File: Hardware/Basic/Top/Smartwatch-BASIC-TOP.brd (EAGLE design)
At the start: 38 x 38 mm, 59 parts, among them SW6 SWITCH.MOM, SW7 SWITCH.MOM, U2 NRF52832_MODULE_MDBT42, U4 FT231XS

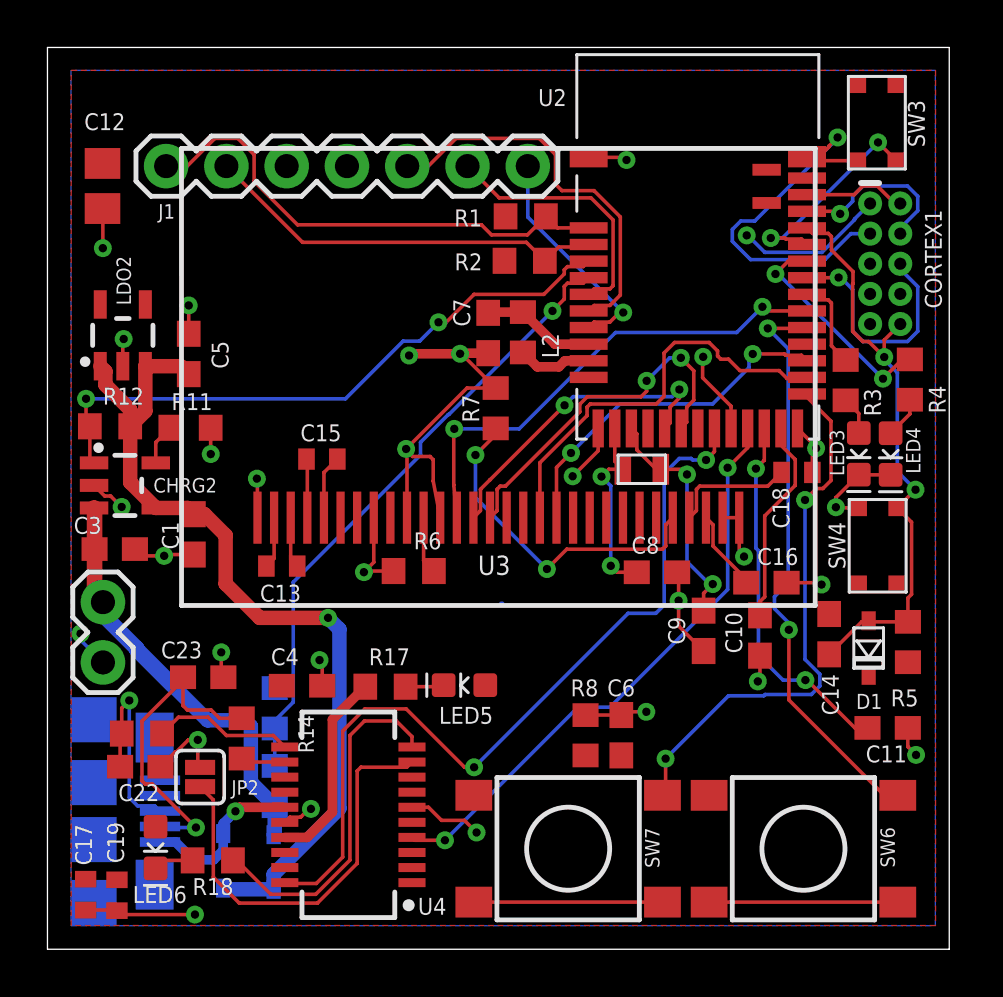
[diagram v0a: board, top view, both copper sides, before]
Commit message: Fixed Top Board Polygon
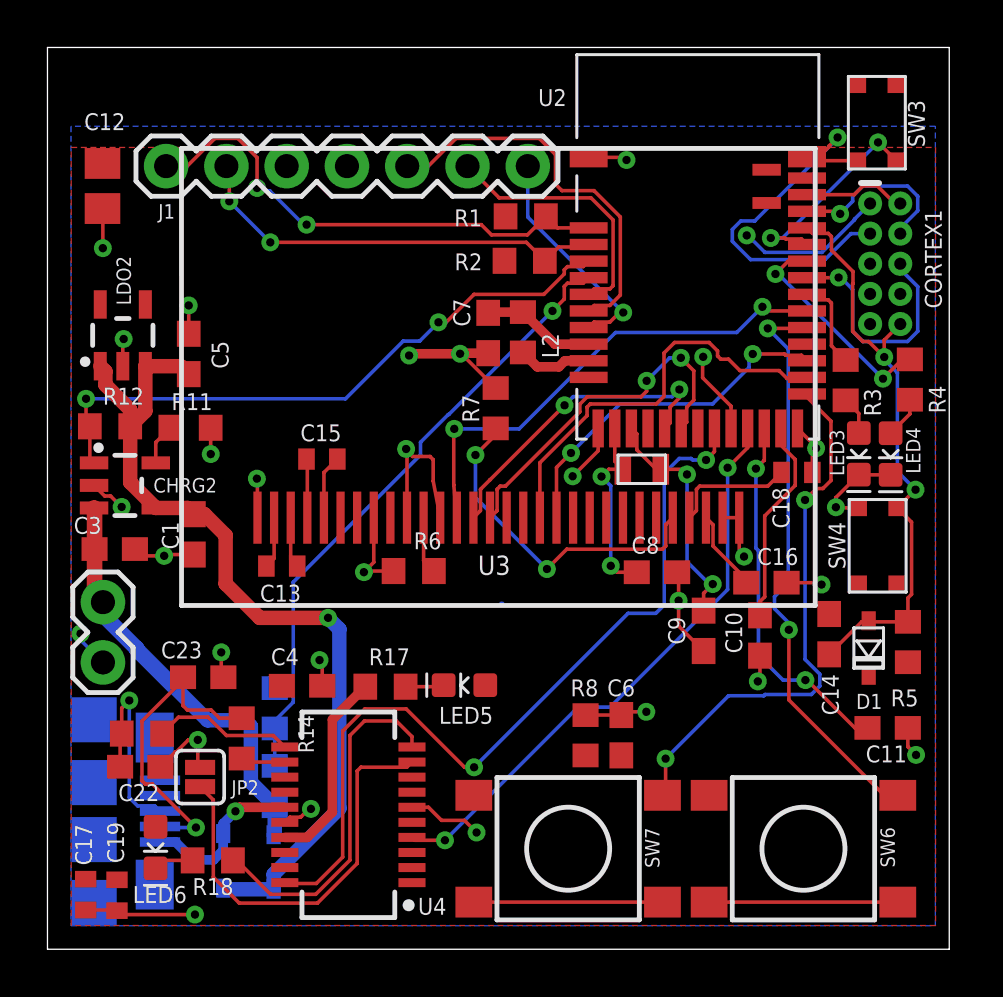
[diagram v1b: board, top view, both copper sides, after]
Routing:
- net GND: track 88.2 -> 83.3 mm
- net SCL: track 17.2 -> 18.0 mm, vias 0 -> 2
- net SDA: vias 0 -> 2
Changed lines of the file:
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@@
 <drawing>
 <settings>
-<setting alwaysvectorfont="yes"/>
+<setting alwaysvectorfont="no"/>
 <setting verticaltext="up"/>
 </settings>
@@
 <wire x1="33.29431875" y1="34.17755625" x2="29.80478125" y2="30.68801875" width="0.1524" layer="16"/>
 <wire x1="29.80478125" y1="30.68801875" x2="29.21519375" y2="30.68801875" width="0.1524" layer="16"/>
-<wire x1="15.113" y1="21.082" x2="17.68004375" y2="23.64904375" width="0.1524" layer="1"/>
-<wire x1="17.68004375" y1="23.64904375" x2="18.887659375" y2="23.64904375" width="0.1524" layer="1"/>
 <wire x1="17.387059375" y1="25.092659375" x2="15.313659375" y2="25.092659375" width="0.4064" layer="1"/>
 <wire x1="15.313659375" y1="25.092659375" x2="15.24" y2="25.019" width="0.4064" layer="1"/>
@@
 <via x="36.601403125" y="8.188959375" extent="1-16" drill="0.35"/>
 <polygon width="0.1524" layer="16" isolate="0.1778">
-<vertex x="0.9906" y="37.0332"/>
+<vertex x="0.9906" y="34.67861875"/>
 <vertex x="0.9906" y="0.9906"/>
 <vertex x="37.4142" y="0.9906"/>
-<vertex x="37.4142" y="37.0332"/>
+<vertex x="37.4142" y="34.67861875"/>
 </polygon>
 <wire x1="31.145615625" y1="15.44699375" x2="32.5386875" y2="15.44699375" width="0.1524" layer="1"/>
@@
 <contactref element="R2" pad="2"/>
 <polygon width="0.1524" layer="1">
-<vertex x="1" y="37.035559375"/>
-<vertex x="37.421640625" y="37.035559375"/>
+<vertex x="1" y="33.786896875"/>
+<vertex x="37.421640625" y="33.786896875"/>
 <vertex x="37.421640625" y="1"/>
 <vertex x="1" y="1"/>
@@
 <contactref element="J1" pad="1"/>
 <wire x1="7.05603125" y1="34.1684" x2="8.02396875" y2="34.1684" width="0.1524" layer="1"/>
-<wire x1="8.02396875" y1="34.1684" x2="8.7084" y2="33.48396875" width="0.1524" layer="1"/>
+<wire x1="8.02396875" y1="34.1684" x2="8.832859375" y2="33.359509375" width="0.1524" layer="1"/>
 <wire x1="5" y1="33" x2="5.88763125" y2="33" width="0.1524" layer="1"/>
 <wire x1="5.88763125" y1="33" x2="7.05603125" y2="34.1684" width="0.1524" layer="1"/>
-<wire x1="8.7084" y1="33.48396875" x2="8.7084" y2="32.35831875" width="0.1524" layer="1"/>
-<wire x1="8.7084" y1="32.35831875" x2="10.53871875" y2="30.528" width="0.1524" layer="1"/>
-<wire x1="18.28631875" y1="30.528" x2="18.70975625" y2="30.1045625" width="0.1524" layer="1"/>
+<wire x1="8.832859375" y1="33.359509375" x2="8.832859375" y2="32.07891875" width="0.1524" layer="1"/>
+<wire x1="10.91971875" y1="30.533078125" x2="10.79525625" y2="30.533078125" width="0.1524" layer="16"/>
+<wire x1="10.79525625" y1="30.533078125" x2="9.373878125" y2="31.95445625" width="0.1524" layer="16"/>
+<wire x1="9.373878125" y1="31.95445625" x2="8.957321875" y2="31.95445625" width="0.1524" layer="16"/>
+<wire x1="8.832859375" y1="32.07891875" x2="8.957321875" y2="31.95445625" width="0.1524" layer="16"/>
+<wire x1="18.281240625" y1="30.533078125" x2="18.70975625" y2="30.1045625" width="0.1524" layer="1"/>
 <wire x1="18.70975625" y1="30.1045625" x2="20.22584375" y2="30.1045625" width="0.1524" layer="1"/>
 <wire x1="20.22584375" y1="30.1045625" x2="21.004440625" y2="30.883159375" width="0.1524" layer="1"/>
-<wire x1="10.53871875" y1="30.528" x2="18.28631875" y2="30.528" width="0.1524" layer="1"/>
+<wire x1="10.91971875" y1="30.533078125" x2="18.281240625" y2="30.533078125" width="0.1524" layer="1"/>
 <wire x1="21.004440625" y1="30.883159375" x2="21.4906" y2="30.397" width="0.1524" layer="1"/>
 <wire x1="21.4906" y1="30.397" x2="22.806" y2="30.397" width="0.1524" layer="1"/>
+<via x="8.832859375" y="32.07891875" extent="1-16" drill="0.35"/>
+<via x="10.91971875" y="30.533078125" extent="1-16" drill="0.35"/>
 </signal>
 <signal name="SCL">
@@
 <contactref element="J1" pad="2"/>
 <wire x1="22.806" y1="29.697" x2="22.7016" y2="29.5926" width="0.1524" layer="1"/>
-<wire x1="7.54" y1="33" x2="10.7512375" y2="29.7887625" width="0.1524" layer="1"/>
+<wire x1="9.389796875" y1="29.7887625" x2="7.66191875" y2="31.516640625" width="0.1524" layer="16"/>
+<wire x1="7.54" y1="33" x2="7.66191875" y2="32.87808125" width="0.1524" layer="1"/>
+<wire x1="7.66191875" y1="32.87808125" x2="7.66191875" y2="31.516640625" width="0.1524" layer="1"/>
 <wire x1="20.180121875" y1="29.7887625" x2="20.958721875" y2="29.0101625" width="0.1524" layer="1"/>
-<wire x1="10.7512375" y1="29.7887625" x2="20.180121875" y2="29.7887625" width="0.1524" layer="1"/>
+<wire x1="9.389796875" y1="29.7887625" x2="20.180121875" y2="29.7887625" width="0.1524" layer="1"/>
 <wire x1="21.541159375" y1="29.5926" x2="20.958721875" y2="29.0101625" width="0.1524" layer="1"/>
 <wire x1="22.7016" y1="29.5926" x2="21.541159375" y2="29.5926" width="0.1524" layer="1"/>
+<via x="9.389796875" y="29.7887625" extent="1-16" drill="0.35"/>
+<via x="7.66191875" y="31.516640625" extent="1-16" drill="0.35"/>
 </signal>
 <signal name="SCK">

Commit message: Top board fixed some traces
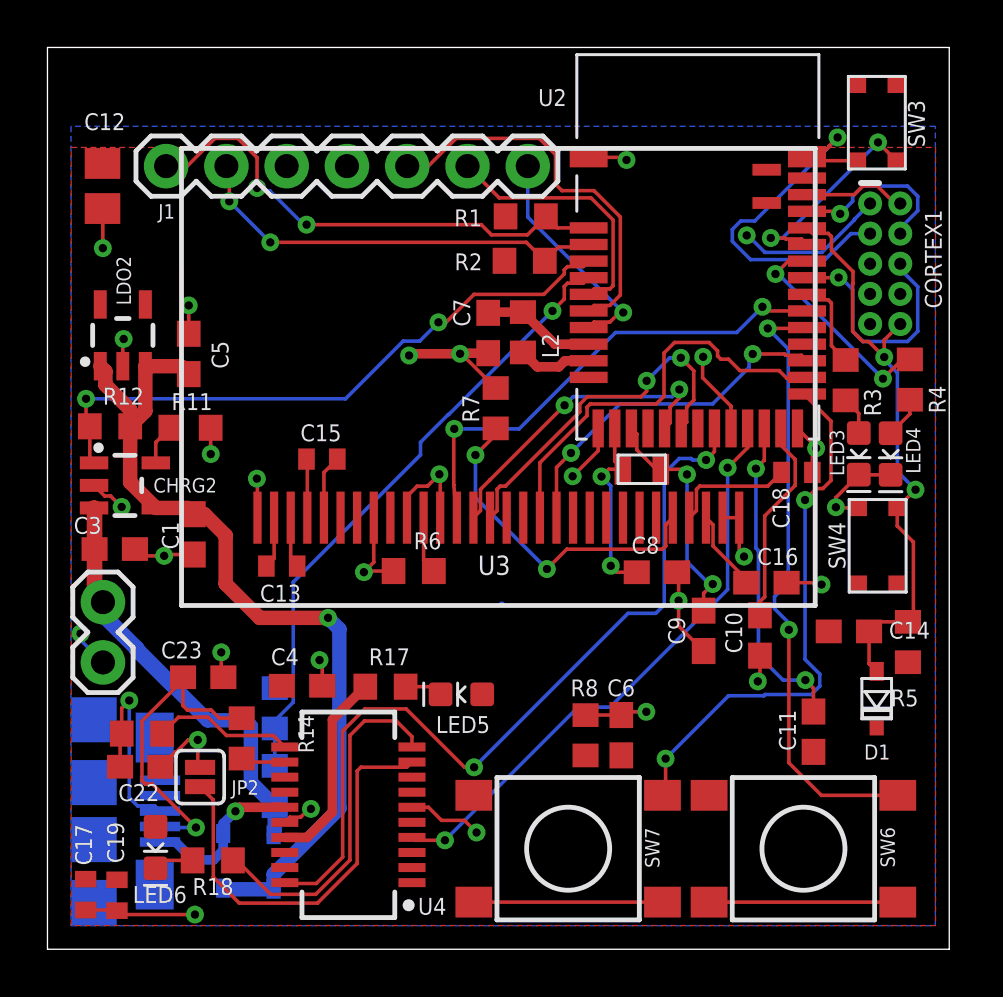
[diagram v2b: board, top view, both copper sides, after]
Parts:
- moved C11 3.13 mm to (32.3, 9.17), turned to 270 degrees
- moved D1 2.16 mm to (34.9, 10.6)
- moved C14 0.84 mm to (33.8, 13.4), turned to 0 degrees
- moved LED5 0.41 mm to (17.4, 10.7)
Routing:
- net GND: track 83.3 -> 79.9 mm, vias 29 -> 28
- net P0.09/NFC1: track 15.6 -> 13.6 mm
- net D15/SW2: track 24.4 -> 26.0 mm

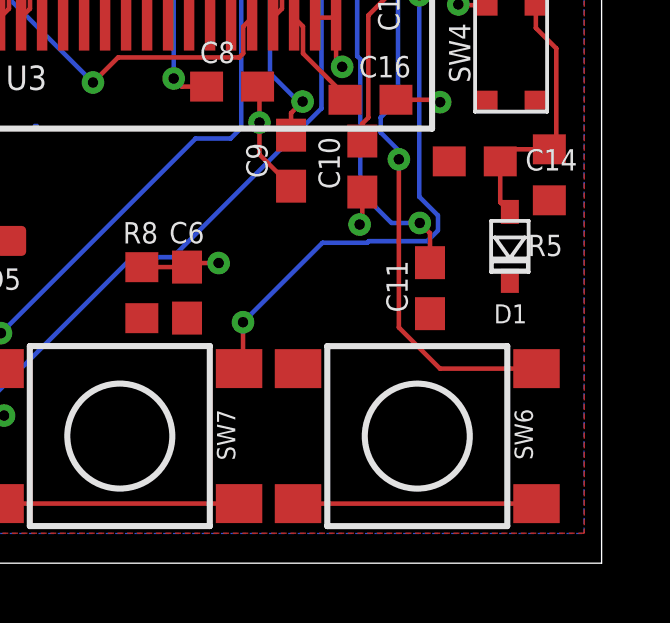
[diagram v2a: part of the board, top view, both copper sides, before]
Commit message: Top Board- Minor problems correct
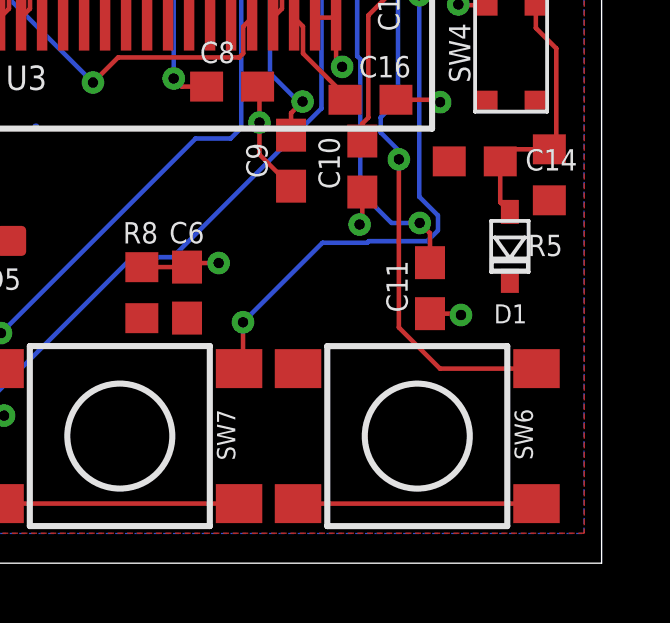
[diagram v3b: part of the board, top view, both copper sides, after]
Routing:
- net GND: track 79.9 -> 81.0 mm, vias 28 -> 29
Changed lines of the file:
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@@
 <wire x1="16.55" y1="18.186" x2="16.55" y2="19.9788625" width="0.1524" layer="1"/>
 <wire x1="16.55" y1="19.9788625" x2="16.5136625" y2="20.0152" width="0.1524" layer="1"/>
-<wire x1="29.9339" y1="11.287759375" x2="32.279365625" y2="8.317840625" width="0" layer="19" extent="1-1"/>
+<wire x1="32.279365625" y1="8.317840625" x2="33.267040625" y2="8.317840625" width="0.1524" layer="1"/>
+<wire x1="33.267040625" y1="8.317840625" x2="33.3121" y2="8.27278125" width="0.1524" layer="1"/>
+<via x="33.3121" y="8.27278125" extent="1-16" drill="0.35"/>
 </signal>
 <signal name="N$4">
